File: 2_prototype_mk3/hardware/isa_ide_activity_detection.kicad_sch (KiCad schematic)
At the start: 13 parts, among them J3 Bus_ISA_8bit, U6 74LS573, U7 74LS573, U8 ATF22V10C-10PU

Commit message: MKIII design refinements
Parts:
- J3: footprint Connector_PCBEdge:BUS_AT -> HDDSyncMKIII:BUS_AT_8bit
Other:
- title: (none) -> ISA IDE activity detection
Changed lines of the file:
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@@
 	(generator_version "9.0")
 	(paper "A4")
+	(title_block
+		(title "ISA IDE activity detection")
+	)
 	(rectangle
 		(start 198.12 125.73)
@@
 			)
 		)
-		(property "Footprint" "Connector_PCBEdge:BUS_AT"
+		(property "Footprint" "HDDSyncMKIII:BUS_AT_8bit"
 			(at 101.6 71.12 0)
 			(effects

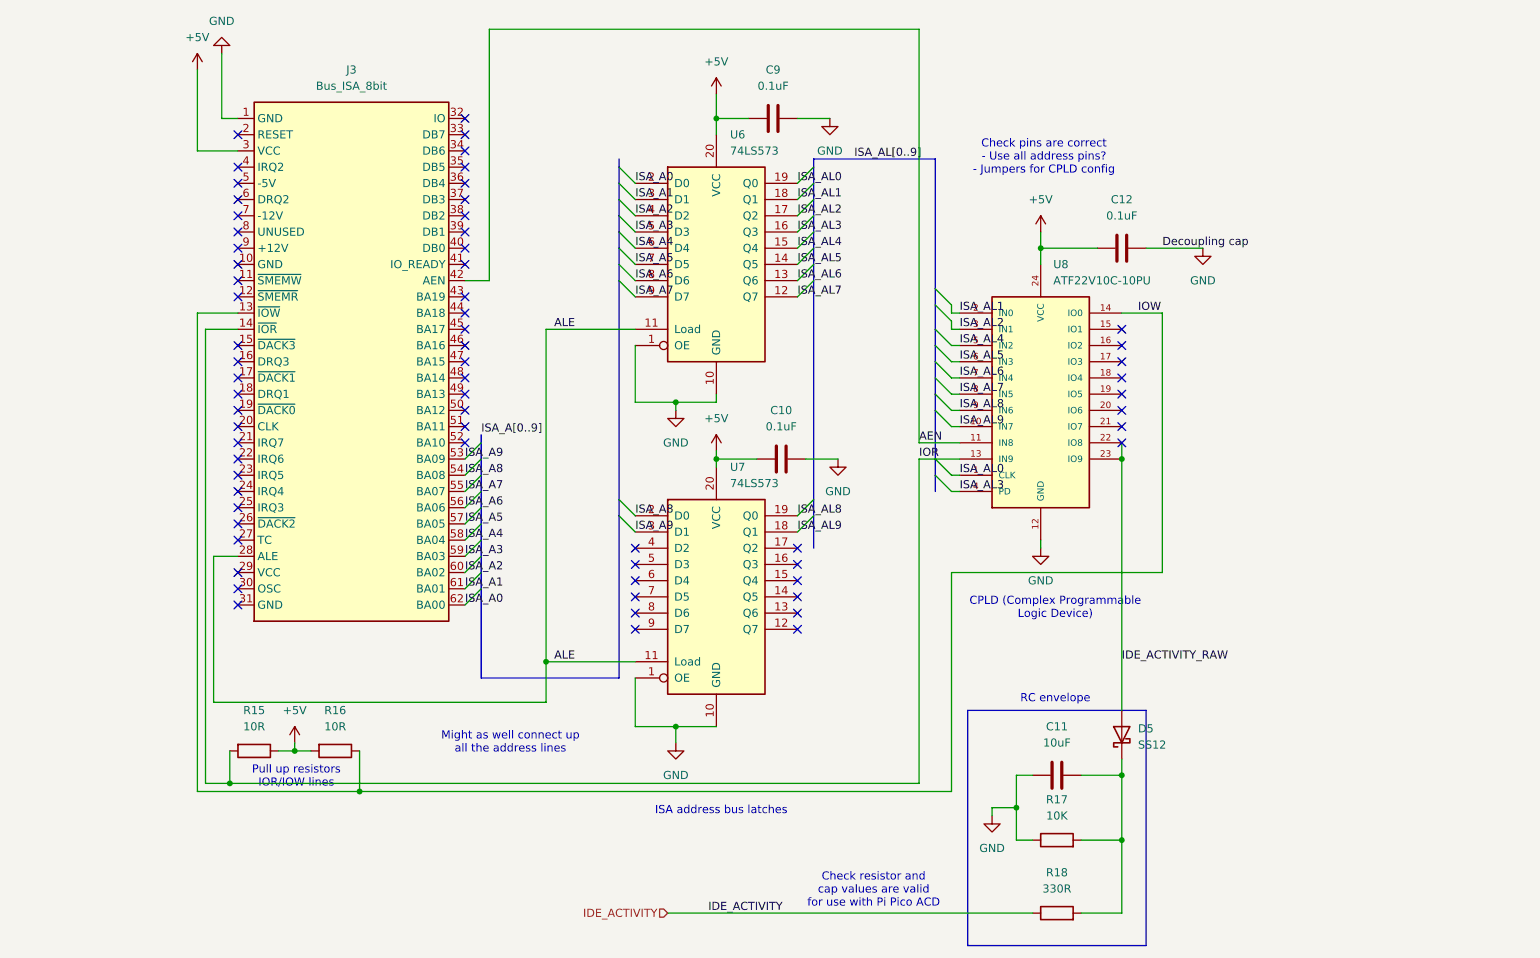
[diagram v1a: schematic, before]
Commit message: Add net classes for power
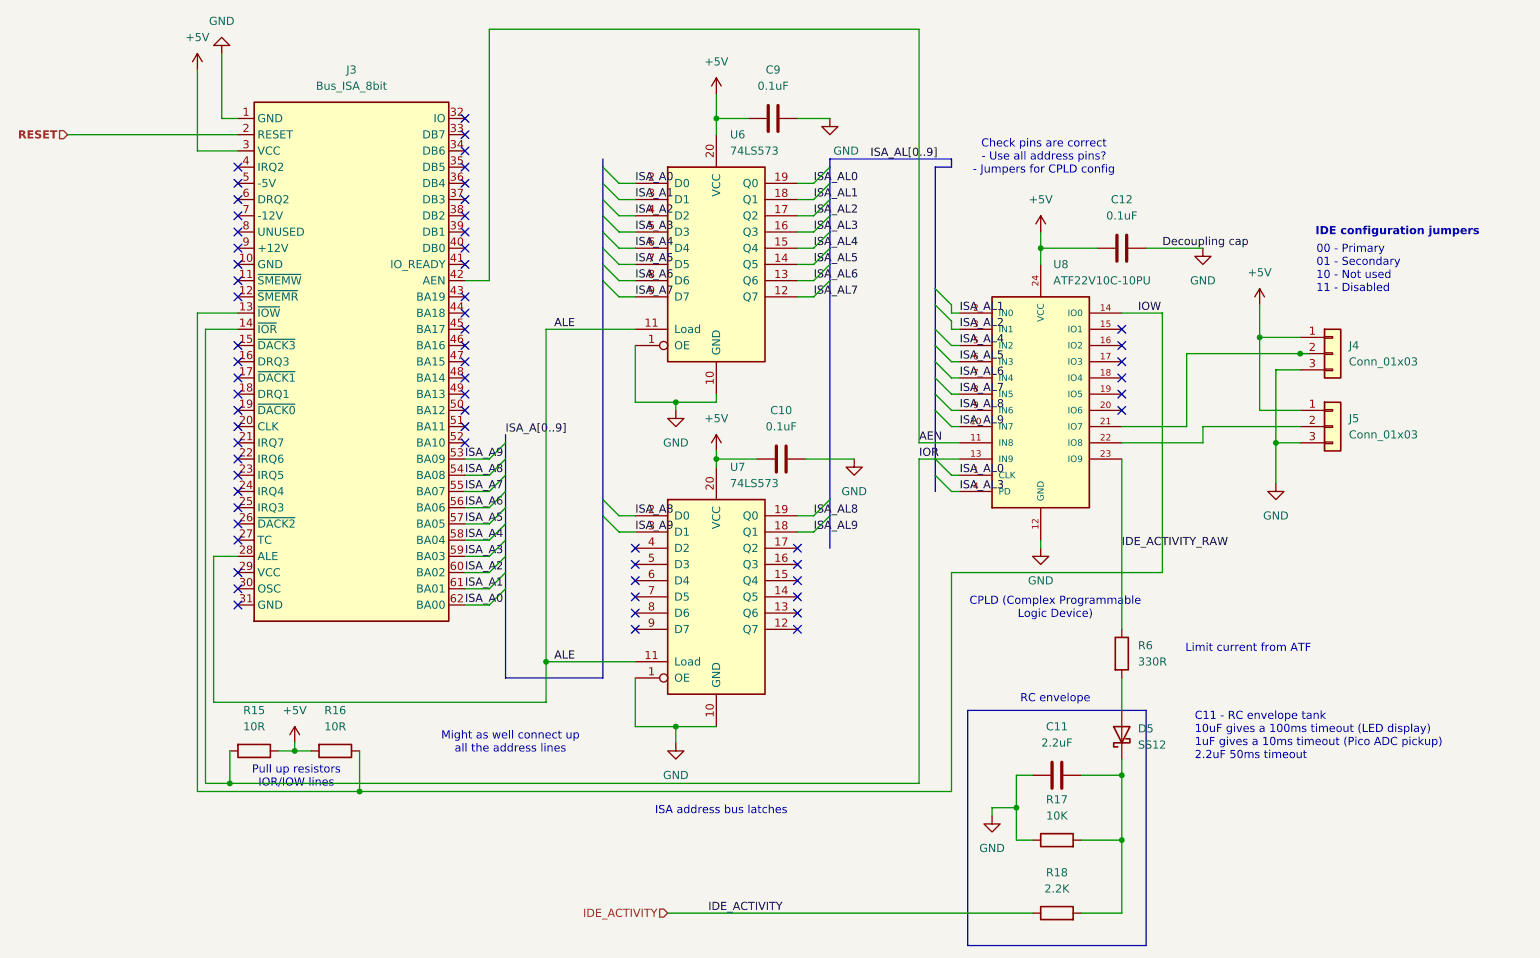
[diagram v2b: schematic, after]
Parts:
- added J4, J5: Conn_01x03, Connector_PinHeader_2.54mm:PinHeader_1x03_P2.54mm_Vertical, symbol Connector_Generic:Conn_01x03
- added R6: 330R, Resistor_SMD:R_0603_1608Metric, symbol Device:R
- C11: value 10uF -> 2.2uF
- R18: value 330R -> 2.2K
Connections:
- net +5V: now also J4.1 (Pin_1), J5.1 (Pin_1)
- net GND: now also J4.3 (Pin_3), J5.3 (Pin_3)
- net IDE_ACTIVITY_RAW: now also R6.1; no longer D5.2 (A), U8.22 (IO8)
- net at U8.21 (IO7): now also J4.2 (Pin_2)
- net RESET: now reaches J3.2 (RESET)
- new net: J5.2 (Pin_2), U8.22 (IO8)
- new net: D5.2 (A), R6.2
- no-connect marks 66 -> 63
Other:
- note added: "00 - Primary 01 - Secondary 10 - Not used 11 - Disabled"
- note added: "C11 - RC envelope tank 10uF gives a 100ms timeout (LED display) 1uF gives a 10ms timeout (Pico ADC pickup) 2.2uF 50ms timeout"
- note added: "IDE configuration jumpers"
- note added: "Limit current from ATF"
- note removed: "Check resistor and cap values are valid for use with Pi Pico ACD"
- title: ISA IDE activity detection -> (none)

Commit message: MKIII PCB components connected and passing DRC
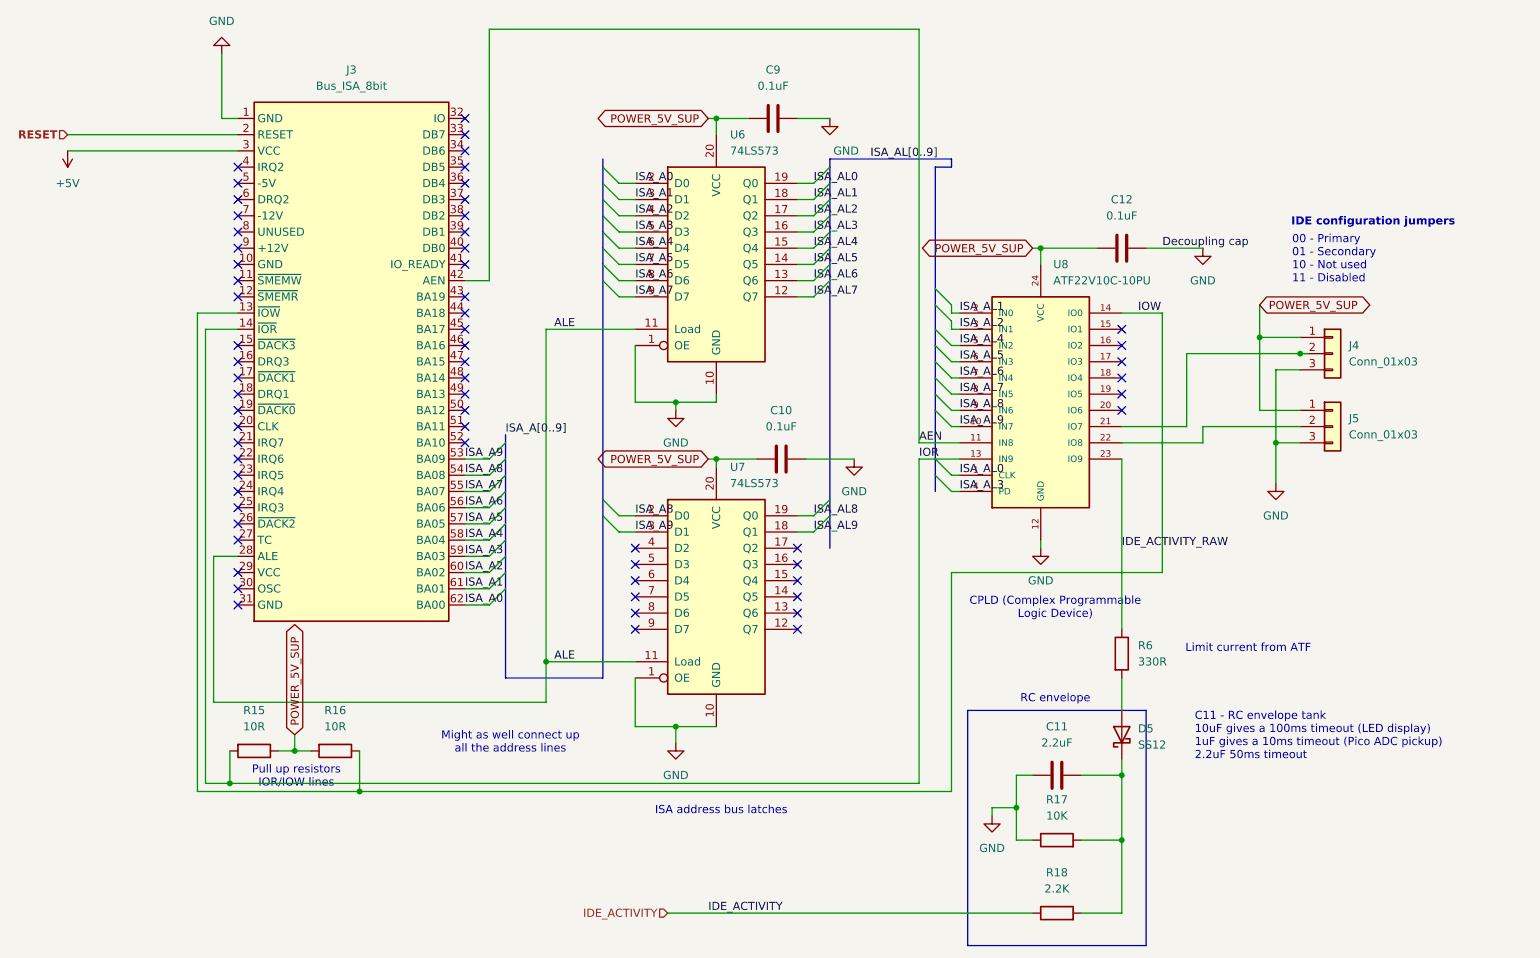
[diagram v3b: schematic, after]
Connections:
- net +5V: no longer C10.1, C12.1, C9.1, J4.1 (Pin_1), J5.1 (Pin_1), R15.1, R16.2, U6.20 (VCC), U7.20 (VCC), U8.24 (VCC)
- new net POWER_5V_SUP: C10.1, C12.1, C9.1, J4.1 (Pin_1), J5.1 (Pin_1), R15.1, R16.2, U6.20 (VCC), U7.20 (VCC), U8.24 (VCC)
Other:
- note removed: "Check pins are correct - Use all address pins? - Jumpers for CPLD config"

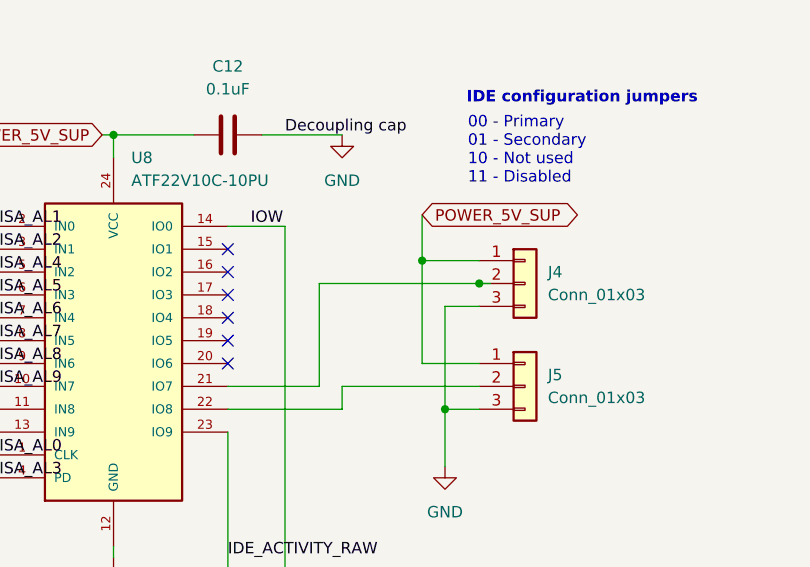
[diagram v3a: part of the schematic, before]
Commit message: Finalise silk screen and tidy up files
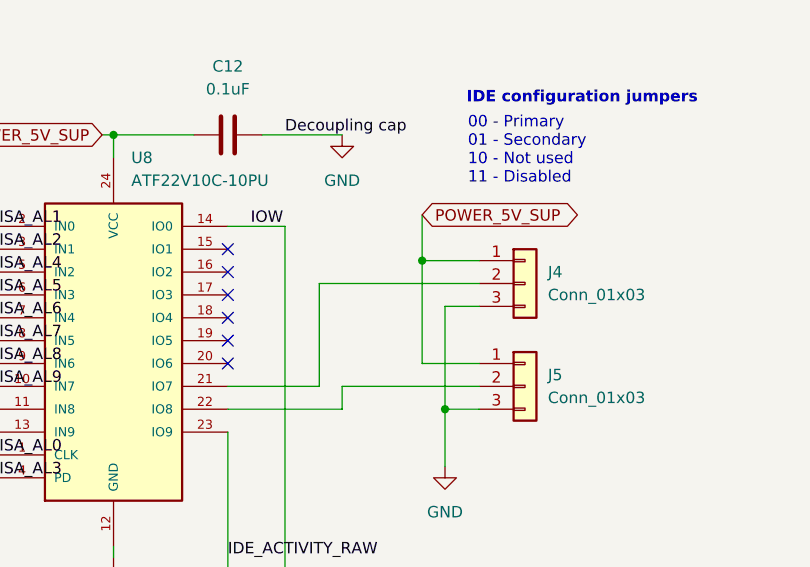
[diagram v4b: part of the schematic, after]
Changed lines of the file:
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@@
-	)
-	(junction
-		(at 250.19 69.85)
-		(diameter 0)
-		(color 0 0 0 0)
 	)
 	(junction
@@
 	(wire
 		(pts
-			(xy 250.19 69.85) (xy 232.41 69.85)
-		)
-		(stroke
-			(width 0)
-			(type default)
-		)
-	)
-	(wire
-		(pts
 			(xy 143.51 43.18) (xy 146.05 43.18)
 		)
@@
 		)
 	)
-	(wire
-		(pts
-			(xy 251.46 69.85) (xy 250.19 69.85)
-		)
-		(stroke
-			(width 0)
-			(type default)
-		)
-	)
 	(bus
 		(pts
@@
 		)
 		(stroke
+			(width 0)
+			(type default)
+		)
+	)
+	(wire
+		(pts
+			(xy 232.41 69.85) (xy 250.19 69.85)
+		)
+		(stroke

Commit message: Add manufacturer part nu bers
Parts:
- C10, C12, C9: Manufacturer_Part_Number (none) -> CL10B104KO8NNNC
- C11: Manufacturer_Part_Number (none) -> CL31B225KCHNNNE
- D5: Manufacturer_Part_Number (none) -> SS12
- R15, R16: Manufacturer_Part_Number (none) -> RC0603FR-0710RL
- R17: Manufacturer_Part_Number (none) -> RC0603FR-0710KL
- R18: Manufacturer_Part_Number (none) -> RC0603FR-072K2L
- R6: Manufacturer_Part_Number (none) -> RC0603FR-07330RL
- U6, U7: Manufacturer_Part_Number (none) -> SN74HCT573APWR
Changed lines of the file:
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@@
+			)
+		)
+		(property "Manufacturer_Part_Number" "CL10B104KO8NNNC"
+			(at 222.25 53.34 90)
+			(effects
+				(font
+					(size 1.27 1.27)
+				)
+				(hide yes)
 			)
 		)
@@
 			)
 		)
+		(property "Manufacturer_Part_Number" "RC0603FR-0710RL"
+			(at 86.36 132.08 90)
+			(effects
+				(font
+					(size 1.27 1.27)
+				)
+				(hide yes)
+			)
+		)
 		(pin "2"
 		)
@@
 			)
 		)
+		(property "Manufacturer_Part_Number" ""
+			(at 209.55 76.2 0)
+			(effects
+				(font
+					(size 1.27 1.27)
+				)
+				(hide yes)
+			)
+		)
 		(pin "13"
 		)
@@
 			)
 		)
+		(property "Manufacturer_Part_Number" "CL10B104KO8NNNC"
+			(at 168.91 86.36 90)
+			(effects
+				(font
+					(size 1.27 1.27)
+				)
+				(hide yes)
+			)
+		)
 		(pin "1"
 		)
@@
 			)
 		)
+		(property "Manufacturer_Part_Number" "SS12"
+			(at 222.25 129.54 90)
+			(effects
+				(font
+					(size 1.27 1.27)
+				)
+				(hide yes)
+			)
+		)
 		(pin "2"
 		)
@@
 			)
 		)
+		(property "Manufacturer_Part_Number" "SN74HCT573APWR"
+			(at 158.75 107.95 0)
+			(effects
+				(font
+					(size 1.27 1.27)
+				)
+				(hide yes)
+			)
+		)
 		(pin "11"
 		)
@@
 		)
 		(property "Description" "8-bit ISA-PC bus connector"
+			(at 101.6 71.12 0)
+			(effects
+				(font
+					(size 1.27 1.27)
+				)
+				(hide yes)
+			)
+		)
+		(property "Manufacturer_Part_Number" ""
 			(at 101.6 71.12 0)
 			(effects
@@
 			)
 		)
+		(property "Manufacturer_Part_Number" "RC0603FR-072K2L"
+			(at 212.09 157.48 90)
+			(effects
+				(font
+					(size 1.27 1.27)
+				)
+				(hide yes)
+			)
+		)
 		(pin "2"
 		)
@@
 			)
 		)
+		(property "Manufacturer_Part_Number" "RC0603FR-0710RL"
+			(at 99.06 132.08 90)
+			(effects
+				(font
+					(size 1.27 1.27)
+				)
+				(hide yes)
+			)
+		)
 		(pin "2"
 		)
@@
 			)
 		)
+		(property "Manufacturer_Part_Number" "RC0603FR-07330RL"
+			(at 222.25 116.84 0)
+			(effects
+				(font
+					(size 1.27 1.27)
+				)
+				(hide yes)
+			)
+		)
 		(pin "2"
 		)
@@
 			)
 		)
+		(property "Manufacturer_Part_Number" "CL10B104KO8NNNC"
+			(at 167.64 33.02 90)
+			(effects
+				(font
+					(size 1.27 1.27)
+				)
+				(hide yes)
+			)
+		)
 		(pin "1"
 		)
@@
 			)
 		)
+		(property "Manufacturer_Part_Number" ""
+			(at 255.27 69.85 0)
+			(effects
+				(font
+					(size 1.27 1.27)
+				)
+				(hide yes)
+			)
+		)
 		(pin "3"
 		)
@@
 			)
 		)
+		(property "Manufacturer_Part_Number" "SN74HCT573APWR"
+			(at 158.75 55.88 0)
+			(effects
+				(font
+					(size 1.27 1.27)
+				)
+				(hide yes)
+			)
+		)
 		(pin "11"
 		)
@@
 			)
 		)
+		(property "Manufacturer_Part_Number" ""
+			(at 255.27 81.28 0)
+			(effects
+				(font
+					(size 1.27 1.27)
+				)
+				(hide yes)
+			)
+		)
 		(pin "3"
 		)
@@
 			)
 		)
+		(property "Manufacturer_Part_Number" "RC0603FR-0710KL"
+			(at 212.09 146.05 90)
+			(effects
+				(font
+					(size 1.27 1.27)
+				)
+				(hide yes)
+			)
+		)
 		(pin "2"
 		)
@@
 			(effects
 				(font
+					(size 1.27 1.27)
+				)
+				(hide yes)
+			)
+		)
+		(property "Manufacturer_Part_Number" "CL31B225KCHNNNE"
+			(at 212.09 135.89 90)
+			(effects
+				(font

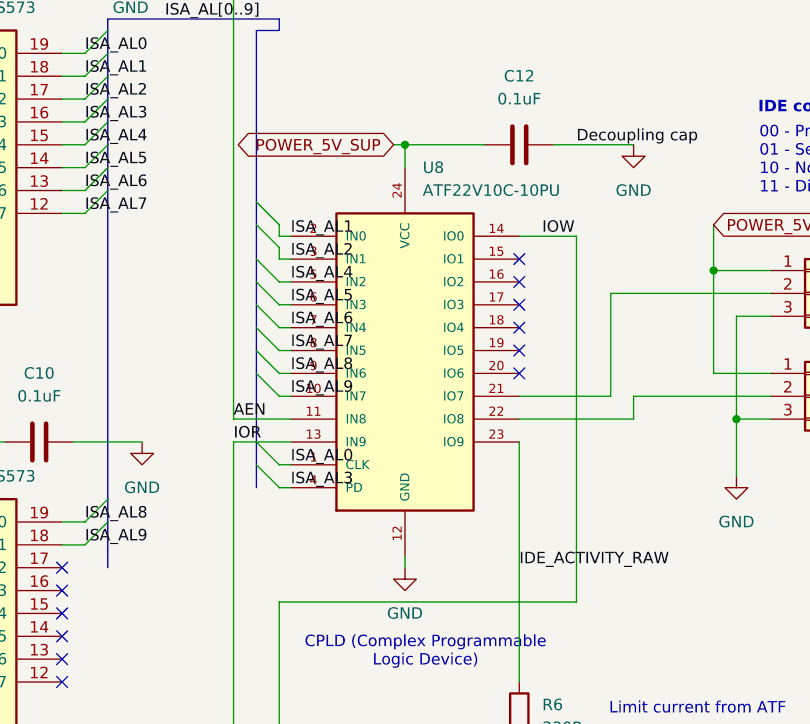
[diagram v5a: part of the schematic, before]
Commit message: Switch SD card reader to better component
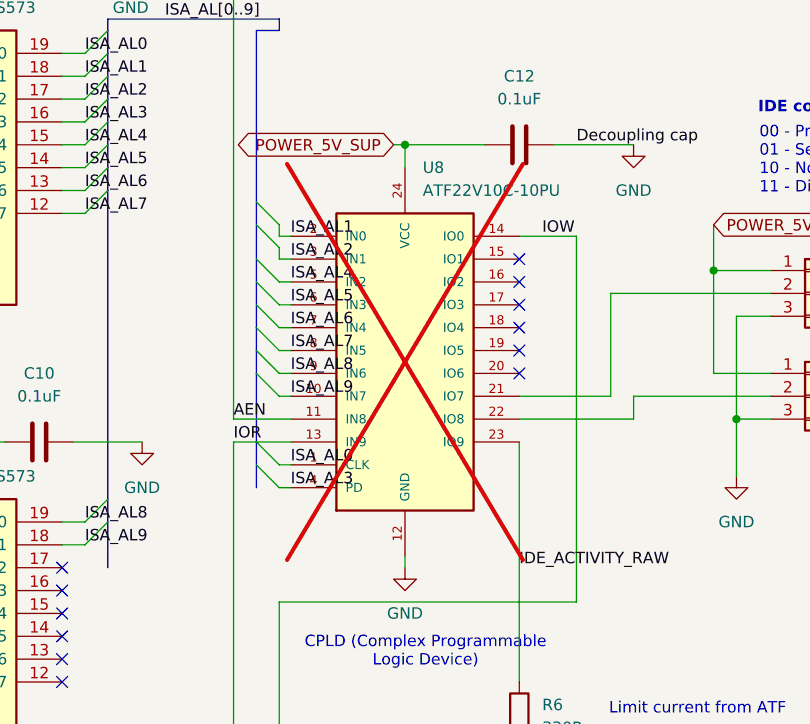
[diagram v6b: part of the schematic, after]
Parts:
- J3: now left out of the parts list
- U6, U7: Manufacturer_Part_Number SN74HCT573APWR -> SN74HC573APWR
- U8: now not fitted; now left out of the parts list
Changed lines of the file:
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@@
 		(unit 1)
 		(exclude_from_sim no)
-		(in_bom yes)
-		(on_board yes)
-		(dnp no)
+		(in_bom no)
+		(on_board yes)
+		(dnp yes)
 		(fields_autoplaced yes)
 		(property "Reference" "U8"
@@
 			)
 		)
-		(property "Manufacturer_Part_Number" "SN74HCT573APWR"
+		(property "Manufacturer_Part_Number" "SN74HC573APWR"
 			(at 158.75 107.95 0)
 			(effects
@@
 		(unit 1)
 		(exclude_from_sim no)
-		(in_bom yes)
+		(in_bom no)
 		(on_board yes)
 		(dnp no)
@@
 			)
 		)
-		(property "Manufacturer_Part_Number" "SN74HCT573APWR"
+		(property "Manufacturer_Part_Number" "SN74HC573APWR"
 			(at 158.75 55.88 0)
 			(effects
